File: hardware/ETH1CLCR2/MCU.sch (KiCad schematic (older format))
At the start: 42 parts, among them J1101 Conn_02x01, J1102 20021111-00010T4LF, U1101 STM32H743ZI, U1102 HDC1080, U1103 24LC08B-E/MS, Y1101 NX3225GD-8MHZ

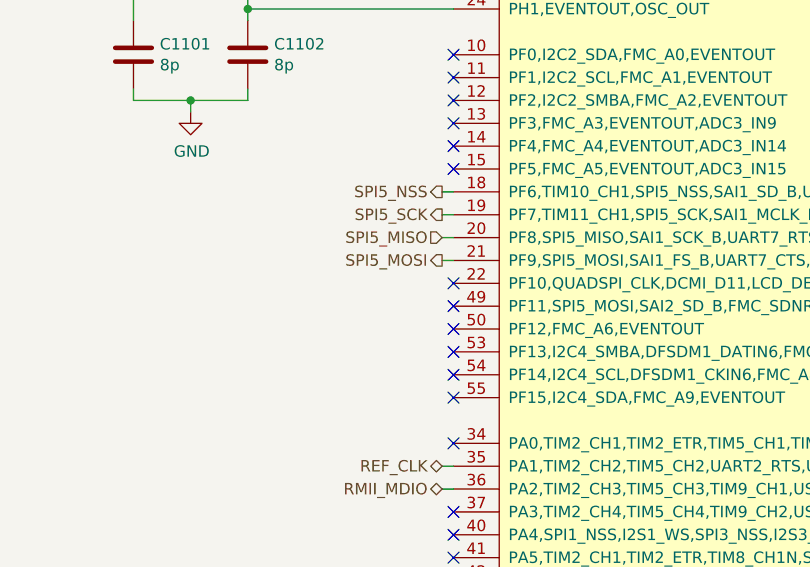
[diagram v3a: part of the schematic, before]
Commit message: Modification in schematic and PCB
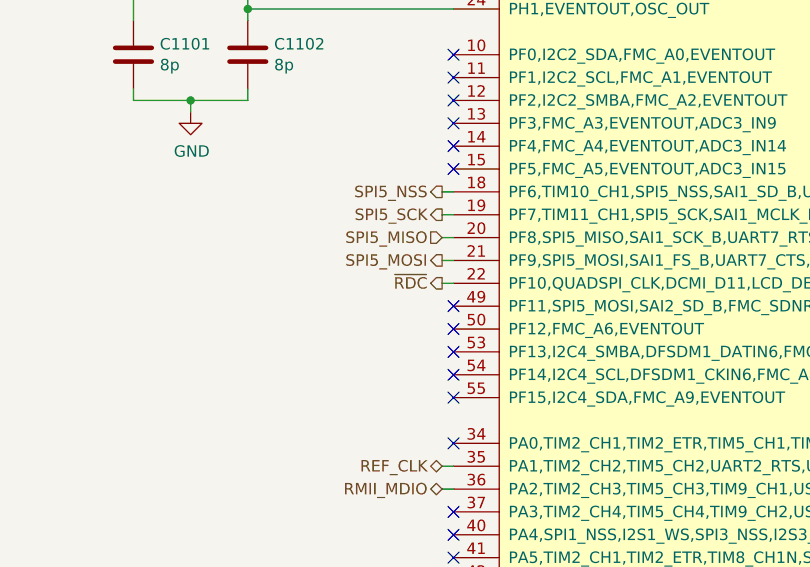
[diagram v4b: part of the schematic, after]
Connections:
- net ~RDC: now reaches U1101.22 (PF10,QUADSPI_CLK,DCMI_D11,LCD_DE,EVENTOUT,ADC3_IN8)
- no-connect marks 49 -> 48
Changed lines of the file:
@@
 Wire Wire Line
 	3600 4700 3650 4700
-NoConn ~ 3650 2500
 NoConn ~ 3650 3200
 NoConn ~ 3650 5100
@@
 Wire Wire Line
 	15100 6800 15050 6800
+Text HLabel 3600 2500 0    50   Output ~ 0
+~RDC
+Wire Wire Line
+	3650 2500 3600 2500
 $EndSCHEMATC

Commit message: PCB done
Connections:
- net CXN_REL1: now also U1101.70 (PB11,TIM2_CH4,I2C2_SDA,DFSDM1_CKIN7,USART3_RX,OTG_HS_ULPI_D4,ETH_MII_TX_EN,ETH_RMII_TX_EN,_DSI_TE,LCD_G5,EVENTOUT); no longer U1101.66 (PE13,TIM1_CH3,SPI4_MISO,DFSDM1_CKIN5,SAI2_FS_B,FMC_D10,LCD_DE,EVENTOUT)
- net CXN_REL2: now also U1101.69 (PB10,TIM2_CH3,I2C2_SCL,SPI2_SCK,I2S2_CK,DFSDM1_DATIN7,USART3_TX,QUADSPI_BK1_NCS,OTG_HS_ULPI_D3,ETH_MII_RX_ER,LCD_G4,EVENTOUT); no longer U1101.67 (PE14,TIM1_CH4,SPI4_MOSI,SAI2_MCLK_B,FMC_D11,LCD_CLK,EVENTOUT)
- net CXN_REL4: now also U1101.67 (PE14,TIM1_CH4,SPI4_MOSI,SAI2_MCLK_B,FMC_D11,LCD_CLK,EVENTOUT); no longer U1101.69 (PB10,TIM2_CH3,I2C2_SCL,SPI2_SCK,I2S2_CK,DFSDM1_DATIN7,USART3_TX,QUADSPI_BK1_NCS,OTG_HS_ULPI_D3,ETH_MII_RX_ER,LCD_G4,EVENTOUT)
- net CXN_REL5: now also U1101.66 (PE13,TIM1_CH3,SPI4_MISO,DFSDM1_CKIN5,SAI2_FS_B,FMC_D10,LCD_DE,EVENTOUT); no longer U1101.70 (PB11,TIM2_CH4,I2C2_SDA,DFSDM1_CKIN7,USART3_RX,OTG_HS_ULPI_D4,ETH_MII_TX_EN,ETH_RMII_TX_EN,_DSI_TE,LCD_G5,EVENTOUT)
- net TRIG_EN: now also U1101.60 (PE9,TIM1_CH1,DFSDM1_CKOUT,UART7_RTS,QUADSPI_BK2_IO2,FMC_D6,EVENTOUT); no longer U1101.63 (PE10,TIM1_CH2N,DFSDM1_DATIN4,UART7_CTS,QUADSPI_BK2_IO3,FMC_D7,EVENTOUT)
- net TRIG_IN: now also U1101.64 (PE11,TIM1_CH2,SPI4_NSS,DFSDM1_CKIN4,SAI2_SD_B,FMC_D8,LCD_G3,EVENTOUT); no longer U1101.65 (PE12,TIM1_CH3N,SPI4_SCK,DFSDM1_DATIN5,SAI2_SCK_B,FMC_D9,LCD_B4,EVENTOUT)
- net TRIG_OUT: now also U1101.63 (PE10,TIM1_CH2N,DFSDM1_DATIN4,UART7_CTS,QUADSPI_BK2_IO3,FMC_D7,EVENTOUT); no longer U1101.64 (PE11,TIM1_CH2,SPI4_NSS,DFSDM1_CKIN4,SAI2_SD_B,FMC_D8,LCD_G3,EVENTOUT)
- new net CXN_REL6: U1101.65 (PE12,TIM1_CH3N,SPI4_SCK,DFSDM1_DATIN5,SAI2_SCK_B,FMC_D9,LCD_B4,EVENTOUT)
- no-connect marks 48 -> 47
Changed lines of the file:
@@
 Text HLabel 15750 8700 2    50   BiDi ~ 0
 NRST
+Text HLabel 15100 5500 2    50   Output ~ 0
+TRIG_EN
 Text HLabel 15100 5600 2    50   Output ~ 0
-TRIG_EN
-Text HLabel 15100 5700 2    50   Output ~ 0
 TRIG_OUT
-Text HLabel 15100 5800 2    50   Input ~ 0
+Text HLabel 15100 5700 2    50   Input ~ 0
 TRIG_IN
 Wire Wire Line
+	15100 5500 15050 5500
+Wire Wire Line
 	15100 5600 15050 5600
 Wire Wire Line
-	15100 5700 15050 5700
-Wire Wire Line
-	15050 5800 15100 5800
+	15050 5700 15100 5700
 NoConn ~ 15050 2400
 $Comp
@@
 NoConn ~ 3650 5100
 NoConn ~ 3650 5200
-Text HLabel 15100 7400 2    50   Output ~ 0
+Text HLabel 15100 5900 2    50   Output ~ 0
 CXN_REL5
-Text HLabel 15100 7300 2    50   Output ~ 0
+Text HLabel 15100 6000 2    50   Output ~ 0
 CXN_REL4
 Text HLabel 15100 6100 2    50   Output ~ 0
 CXN_REL3
-Text HLabel 15100 6000 2    50   Output ~ 0
+Text HLabel 15100 7300 2    50   Output ~ 0
 CXN_REL2
-Text HLabel 15100 5900 2    50   Output ~ 0
+Text HLabel 15100 7400 2    50   Output ~ 0
 CXN_REL1
 Wire Wire Line
-	15100 7400 15050 7400
-Wire Wire Line
-	15050 7300 15100 7300
-Wire Wire Line
-	15100 6100 15050 6100
-Wire Wire Line
-	15050 6000 15100 6000
-Wire Wire Line
-	15100 5900 15050 5900
+	15100 7300 15050 7300
+Wire Wire Line
+	15050 6100 15100 6100
+Wire Wire Line
+	15100 6000 15050 6000
+Wire Wire Line
+	15050 5900 15100 5900
+Wire Wire Line
+	15100 5800 15050 5800
 Text HLabel 3600 4300 0    50   Output ~ 0
 IRR1
@@
 NoConn ~ 15050 5300
 NoConn ~ 15050 5400
-NoConn ~ 15050 5500
 NoConn ~ 15050 4400
 NoConn ~ 15050 2700
@@
 Wire Wire Line
 	3650 2500 3600 2500
+Text HLabel 15100 5800 2    50   Output ~ 0
+CXN_REL6
+Wire Wire Line
+	15100 7400 15050 7400
 $EndSCHEMATC

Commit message: BOM
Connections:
- net IDIFF1: now also U1101.7 (PC13,EVENTOUT,RTC_TAMP2,RTC_TS,WKUP5); no longer U1101.4 (PE5,TRACED2,TIM9_CH1,SPI4_MISO,SAI1_SCK_A,DFSDM1_CKIN3,FMC_A21,DCMI_D6,LCD_G0,EVENTOUT)
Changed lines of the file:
@@
 Wire Wire Line
 	3650 5500 3600 5500
-Text HLabel 15100 5100 2    50   Output ~ 0
+Text HLabel 3600 6200 0    50   Output ~ 0
 IDIFF1
 Text HLabel 15100 4900 2    50   Output ~ 0
@@
 	15050 4900 15100 4900
 Wire Wire Line
-	15100 5100 15050 5100
+	3600 6200 3650 6200
 NoConn ~ 15050 5300
 NoConn ~ 15050 5400
@@
 NoConn ~ 3650 2800
 NoConn ~ 3650 2700
-NoConn ~ 3650 6200
 NoConn ~ 3650 6300
 NoConn ~ 3650 6400
@@
 Wire Wire Line
 	15100 7400 15050 7400
+NoConn ~ 15050 5100
 $EndSCHEMATC

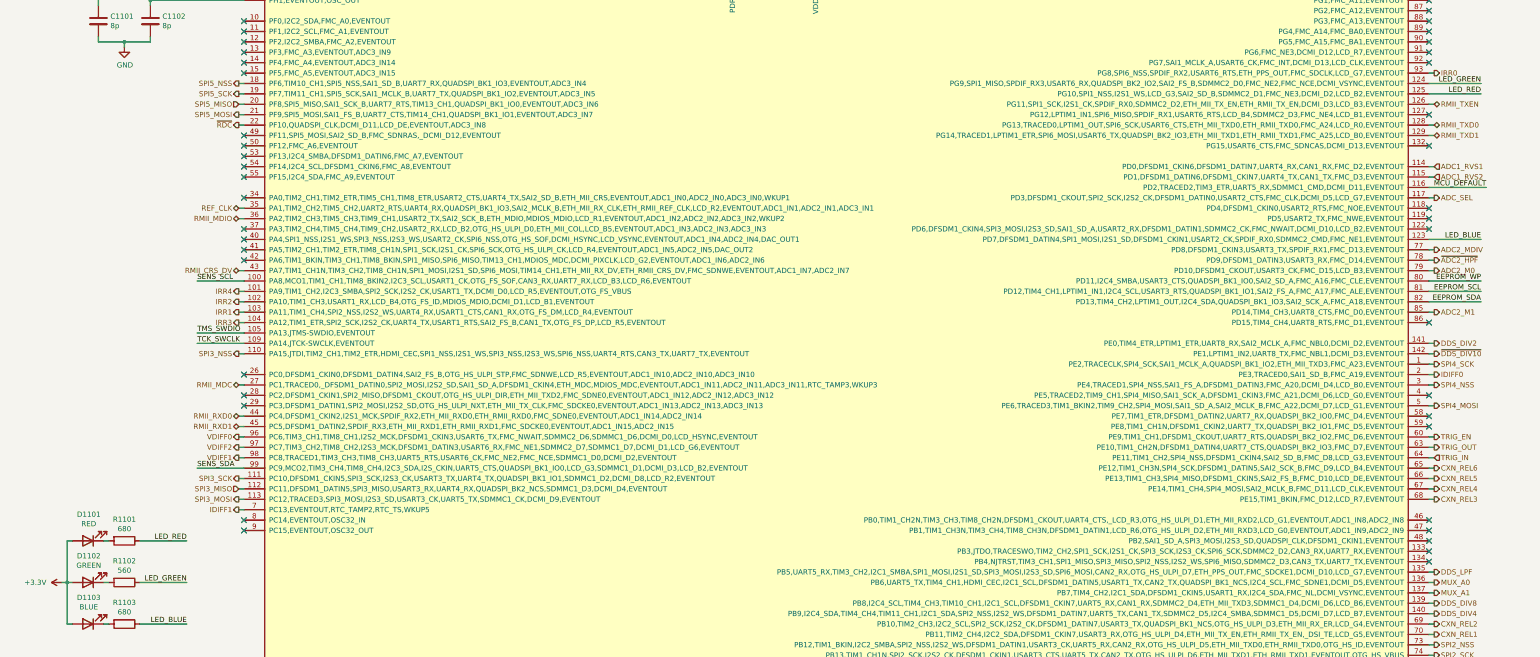
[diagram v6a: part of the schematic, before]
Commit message: Ethernet connection and SCPI commands are working. Swapped red and green LED in the schematic.
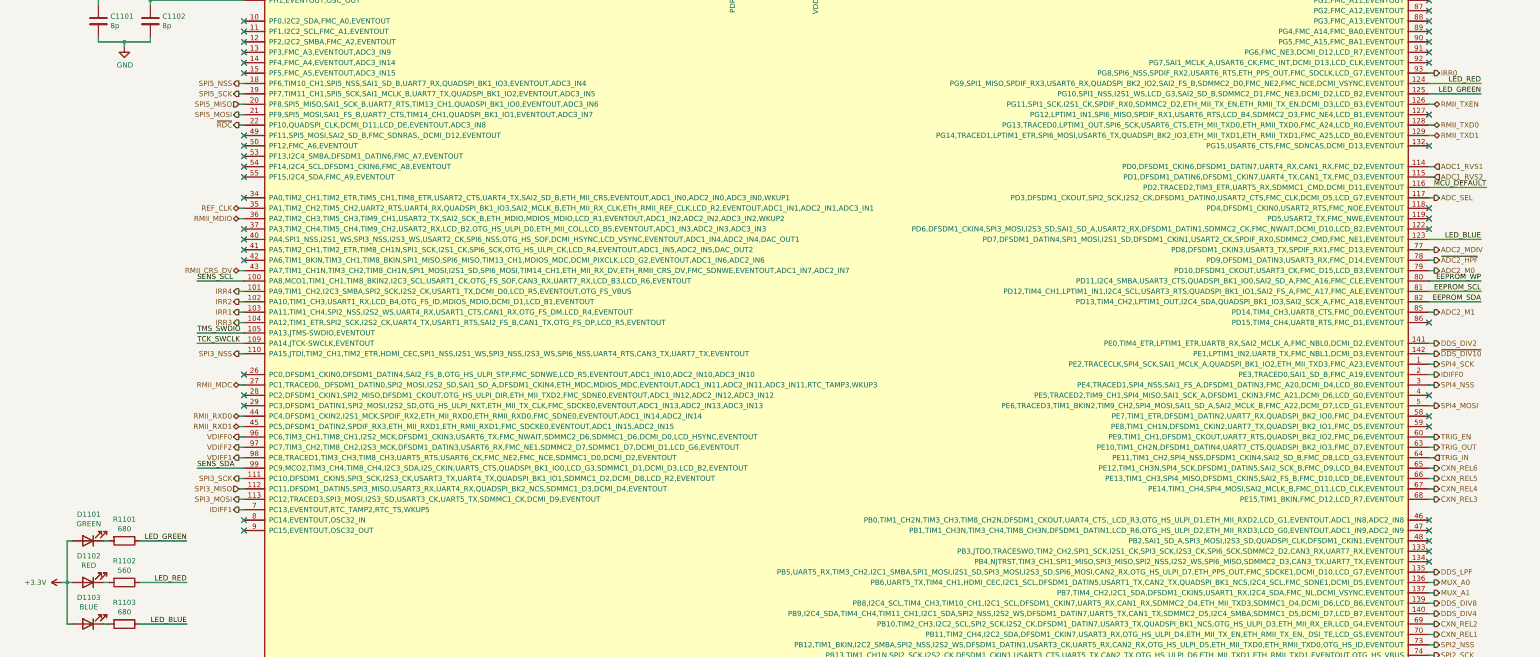
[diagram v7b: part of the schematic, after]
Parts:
- D1101: value RED -> GREEN
- D1102: value GREEN -> RED
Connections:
- net LED_GREEN: now also R1101.1, U1101.125 (PG10,SPI1_NSS,I2S1_WS,LCD_G3,SAI2_SD_B,SDMMC2_D1,FMC_NE3,DCMI_D2,LCD_B2,EVENTOUT); no longer R1102.1, U1101.124 (PG9,SPI1_MISO,SPDIF_RX3,USART6_RX,QUADSPI_BK2_IO2,SAI2_FS_B,SDMMC2_D0,FMC_NE2,FMC_NCE,DCMI_VSYNC,EVENTOUT)
- net LED_RED: now also R1102.1, U1101.124 (PG9,SPI1_MISO,SPDIF_RX3,USART6_RX,QUADSPI_BK2_IO2,SAI2_FS_B,SDMMC2_D0,FMC_NE2,FMC_NCE,DCMI_VSYNC,EVENTOUT); no longer R1101.1, U1101.125 (PG10,SPI1_NSS,I2S1_WS,LCD_G3,SAI2_SD_B,SDMMC2_D1,FMC_NE3,DCMI_D2,LCD_B2,EVENTOUT)
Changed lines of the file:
@@
 P 2150 6500
 F 0 "D1101" H 2143 6245 50  0000 C CNN
-F 1 "RED" H 2143 6336 50  0000 C CNN
+F 1 "GREEN" H 2143 6336 50  0000 C CNN
 F 2 "LED_SMD:LED_0603_1608Metric_Pad1.05x0.95mm_HandSolder" H 2150 6500 50  0001 C CNN
 F 3 "~" H 2150 6500 50  0001 C CNN
@@
 P 2150 6900
 F 0 "D1102" H 2143 6645 50  0000 C CNN
-F 1 "GREEN" H 2143 6736 50  0000 C CNN
+F 1 "RED" H 2143 6736 50  0000 C CNN
 F 2 "LED_SMD:LED_0603_1608Metric_Pad1.05x0.95mm_HandSolder" H 2150 6900 50  0001 C CNN
 F 3 "~" H 2150 6900 50  0001 C CNN
@@
 	2650 6900 3100 6900
 Text Label 3100 6900 2    50   ~ 0
-LED_GREEN
-Text Label 15550 2100 2    50   ~ 0
-LED_GREEN
-Wire Wire Line
-	2650 6500 3100 6500
-Text Label 3100 6500 2    50   ~ 0
 LED_RED
 Text Label 15550 2200 2    50   ~ 0
+LED_GREEN
+Wire Wire Line
+	2650 6500 3100 6500
+Text Label 15550 2100 2    50   ~ 0
 LED_RED
 Text HLabel 15100 3200 2    50   Output ~ 0
@@
 	15100 7400 15050 7400
 NoConn ~ 15050 5100
+Text Label 3100 6500 2    50   ~ 0
+LED_GREEN
 $EndSCHEMATC
